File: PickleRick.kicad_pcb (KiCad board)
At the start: 4 copper layers, 100 x 37 mm, 171 parts, among them J1 RBUS, J10 Conn_Coaxial, J11 Conn_Coaxial, J12 Conn_01x03_Male, J2 Conn_01x02_Male, J3 292227-7, J4 Micro_SD_Card_Det, J5 USB_C_Receptacle_USB2.0, J6 Screw_Terminal_01x08, J7 Conn_01x05_Male, J8 DeployLipo, J9 UCLipo, Q1 PMV20ENR, Q2 NCV8415STT1G, Q3 NCV8415STT1G, Q4 NCV8415STT1G, Q5 NCV8415STT1G, Q6 SI4143DY-T1-GE3, Q7 SI4143DY-T1-GE3, U1 ESP32-S3, U10 NCP1117-3.3_SOT223, U11 XC8111, U12 XC8111, U13 XC8111, U14 LTC4412xS6, U15 MAX77827AEFD+T, U16 SC4215, U17 LTC4412xS6, U18 XC8111, U19 MAX-M10S, U2 DPS310, U20 SN65HVD230, U21 RFM95W-868S2, U3 LTV-247, U4 PCA9534RGVR, U5 PCA9685BS, U6 H3LIS331DLTR, U7 ICM-20608-G, U8 MMC5983MA, U9 XC8111, Y1 40MHz±10ppm

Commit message: made more progress
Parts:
- removed C37: 100nF, Capacitor_SMD:C_0402_1005Metric
- removed R13: 10k, Resistor_SMD:R_0402_1005Metric
- J5: footprint Connector_USB:USB_C_Receptacle_GCT_USB4085 -> Connector_USB:USB_C_Receptacle_Palconn_UTC16-G
- TP7, TP8: moved to F.Cu
- moved TP15 152.0 mm to (123.6, 67.4)
- moved TP6 129.4 mm to (123.5, 75.6)
- moved TP5 118.9 mm to (123.5, 73.6)
- moved TP1 103.5 mm to (136.2, 116.6)
- moved TP4 103.5 mm to (131.8, 116.6)
- moved TP10 103.5 mm to (121.4, 114.7)
- moved TP11 103.5 mm to (155.2, 114.3)
- moved TP12 103.5 mm to (154.7, 117.9)
- moved TP13 103.5 mm to (151.2, 116.8)
- moved TP14 103.5 mm to (158.7, 114.3)
- moved TP3 103.5 mm to (144.1, 116.6)
- moved TP9 103.5 mm to (145.0, 110.1)
- moved C48 67.1 mm to (208.9, 93.7), turned to -90 degrees
- moved C47 63.4 mm to (204.0, 88.9), turned to -90 degrees
- moved C46 61.8 mm to (206.5, 88.8), turned to -90 degrees
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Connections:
- J3 pad 1: +3V3 -> /SD2_DET
- J3 pad 3: /VSPI_MOSI -> /VSPI_MISO
- J3 pad 6: /VSPI_MISO -> /VSPI_MOSI
- J3 pad 7: /SD2_DET -> +3V3
- R10 pad 1: +12V -> +24V
- U1 pad 10: /IMU2_CS -> /SD2_DET
- U1 pad 11: /IMU1_CS -> /SD2_CS
- U1 pad 12: /BARO_CS -> /SD1_CS
- U1 pad 16: /SD2_DET -> /IMU2_CS
- U1 pad 17: /SD2_CS -> /IMU1_CS
- U1 pad 18: /SD1_DET -> /MAG_CS
- U1 pad 19: /SD1_CS -> /BARO_CS
- U1 pad 38: /VSPI_MOSI -> /HSPI_SCLK
- U1 pad 39: /VSPI_SCLK -> /HSPI_MOSI
- U1 pad 40: /VSPI_MISO -> /HSPI_MISO
- U1 pad 41: /HSPI_SCLK -> /VSPI_MISO
- U1 pad 42: /HSPI_MOSI -> /VSPI_SCLK
- U1 pad 43: /HSPI_MISO -> /VSPI_MOSI
- U1 pad 9: /MAG_CS -> /SD1_DET
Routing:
- net /SDA: track 7.53 -> 140.9 mm, vias 0 -> 2
- net /SD1_DET: track 0.45 -> 98.0 mm
- net /SD2_DET: track 0.67 -> 97.4 mm
- net /SD2_CS: track 0.00 -> 67.4 mm
- net /LORA_INT: track 23.1 -> 82.0 mm
- net /SCL: track 194.5 -> 143.7 mm, vias 3 -> 2
- net Net-(D7-Pad3): track 54.1 -> 12.6 mm
- net /SD1_CS: track 3.66 -> 43.6 mm
- net VBUS: track 46.9 -> 7.75 mm
- net /HSPI_MOSI: track 31.2 -> 69.3 mm, vias 2 -> 4
- net /HSPI_MISO: track 35.4 -> 71.8 mm, vias 2 -> 4
- net /HSPI_SCLK: track 28.3 -> 63.1 mm, vias 2 -> 4
- net /LORA_RESET: track 20.4 -> 51.4 mm
- net /BARO_CS: track 0.00 -> 30.3 mm
- net /nukes/Nuke1-: track 0.00 -> 27.9 mm
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
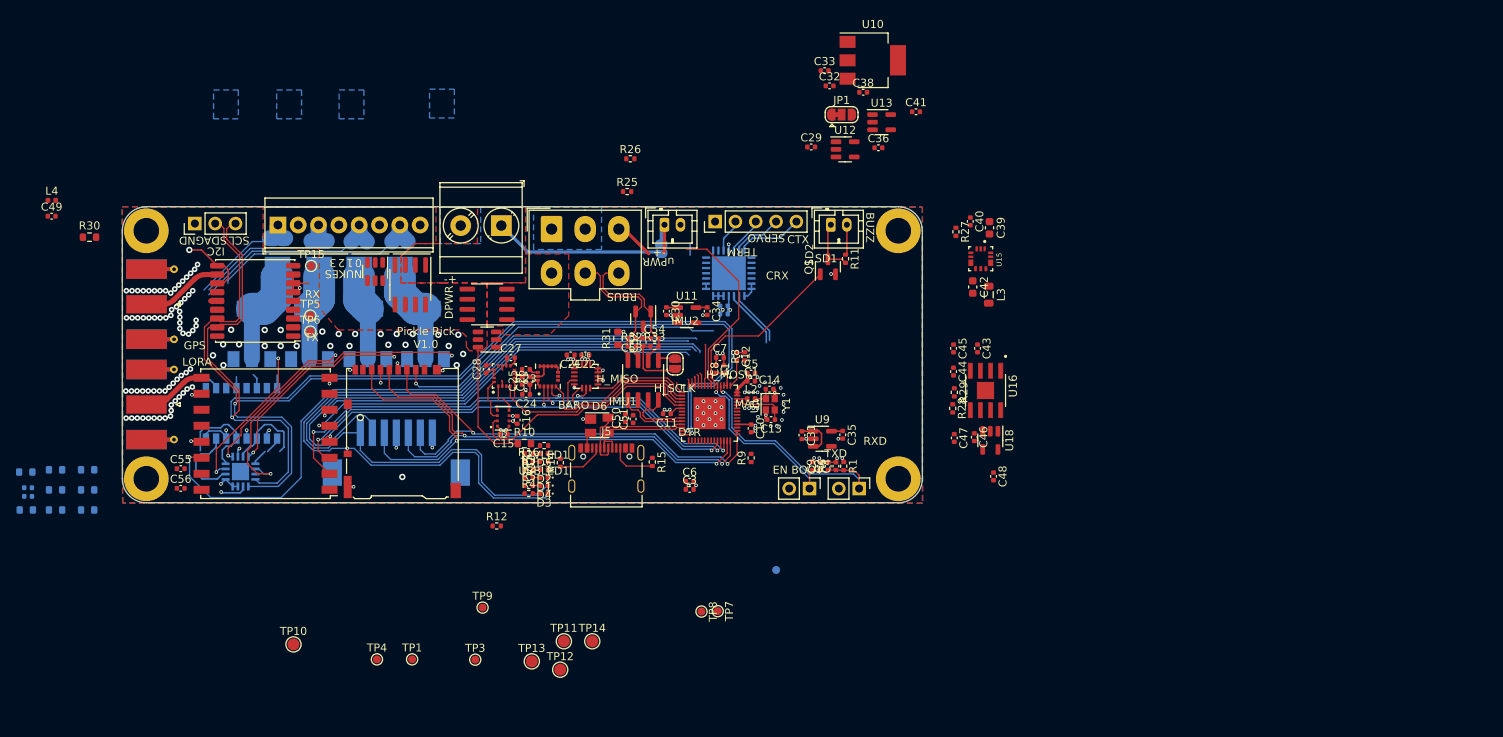
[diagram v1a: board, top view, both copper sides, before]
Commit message: all components basically routed and fitted onto pickle v2
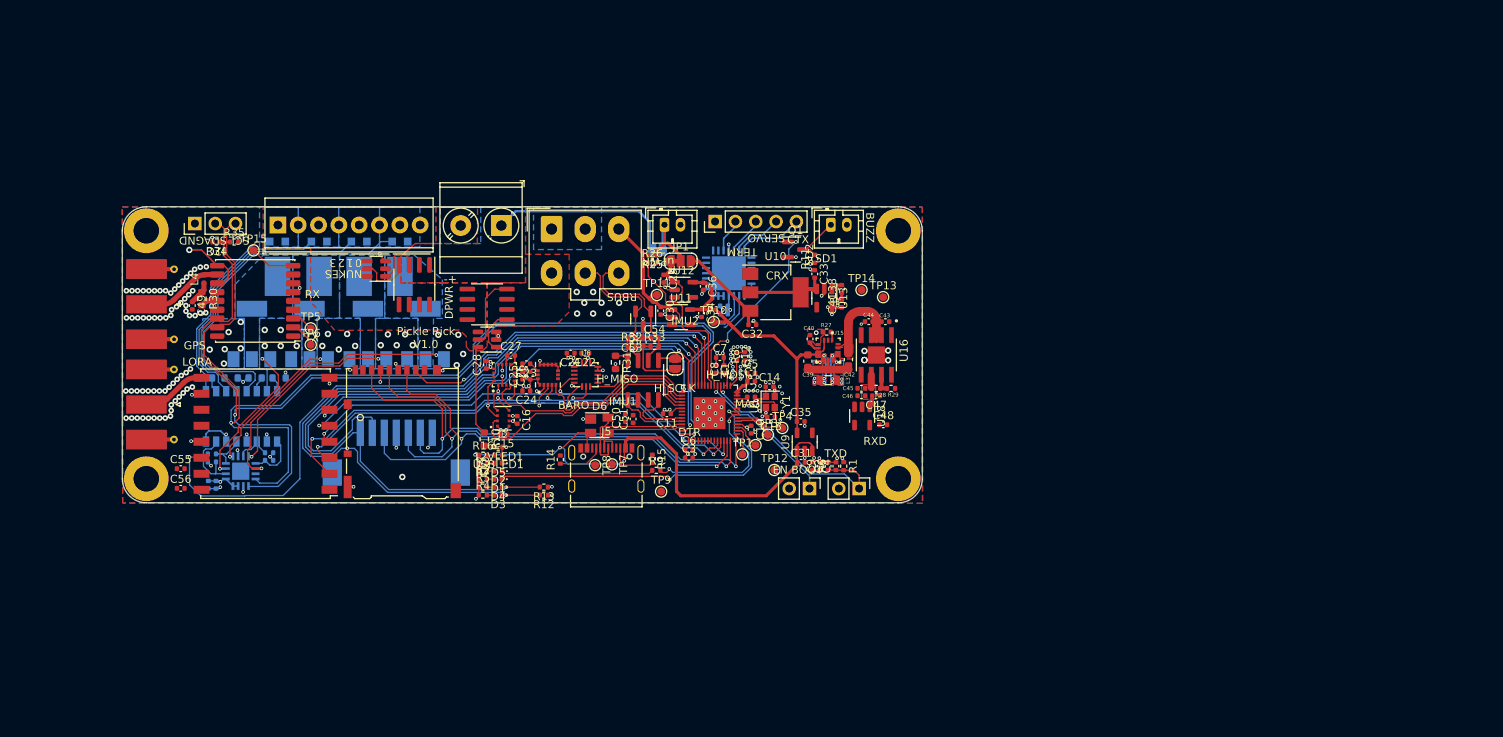
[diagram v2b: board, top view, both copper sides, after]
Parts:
- added R13: 10k, Resistor_SMD:R_0402_1005Metric, F.Cu at (152.7, 95.0)
- added R34: 4.7k, Resistor_SMD:R_0402_1005Metric, F.Cu at (111.8, 64.4)
- added R35: 4.7k, Resistor_SMD:R_0402_1005Metric, F.Cu at (114.0, 64.4)
- R17, R18, R21, R22: footprint Resistor_SMD:R_0603_1608Metric -> Resistor_SMD:R_0402_1005Metric
- TP10, TP11, TP12, TP13, TP14: footprint TestPoint:TestPoint_Pad_D1.5mm -> TestPoint:TestPoint_Pad_D1.0mm
- TP2: moved to F.Cu
- moved TP10 66.2 mm to (173.9, 74.4)
- moved TP13 63.3 mm to (195.1, 71.3)
- moved TP4 58.3 mm to (182.5, 87.7)
- moved TP14 55.3 mm to (192.4, 70.4)
- moved TP1 48.6 mm to (177.5, 91.0)
- moved TP3 46.1 mm to (180.7, 88.5)
- moved TP11 44.8 mm to (166.8, 71.0)
- moved TP12 36.6 mm to (181.5, 92.9)
- moved R23 32.5 mm to (119.6, 81.4), turned to 0 degrees
- moved U10 31.5 mm to (181.7, 70.7)
- moved C32 31.4 mm to (178.8, 74.8), turned to 180 degrees
- moved R20 30.5 mm to (113.6, 81.4), turned to 0 degrees
- moved C39 28.2 mm to (185.7, 79.3)
- moved C36 27.9 mm to (172.6, 70.0), turned to -90 degrees
- moved R24 27.5 mm to (116.6, 81.4)
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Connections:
- J1 pad 3: /RBUS_3.3_IN -> /power/RBUS_3.3V_IN
- J3 pad 3: /VSPI_MISO -> /VSPI_MOSI
- J3 pad 6: /VSPI_MOSI -> /VSPI_MISO
- U1 pad 10: /SD2_DET -> /LORA_INT
- U1 pad 11: /SD2_CS -> /SD1_DET
- U1 pad 12: /SD1_CS -> /SD2_DET
- U1 pad 13: /LORA_CS -> /SD2_CS
- U1 pad 15: /LORA_INT -> /LORA_CS
- U1 pad 38: /HSPI_SCLK -> /HSPI_MOSI
- U1 pad 39: /HSPI_MOSI -> /HSPI_MISO
- U1 pad 40: /HSPI_MISO -> /HSPI_SCLK
- U1 pad 41: /VSPI_MISO -> /VSPI_MOSI
- U1 pad 43: /VSPI_MOSI -> /VSPI_MISO
- U1 pad 9: /SD1_DET -> /SD1_CS
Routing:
- net VBUS: track 7.75 -> 66.1 mm, vias 0 -> 4
- net /RXD: track 0.00 -> 41.3 mm, vias 0 -> 2
- net /power/BBIN: track 2.85 -> 38.6 mm
- net GND: track 65.2 -> 87.5 mm, vias 166 -> 217
- net Net-(R9-Pad2): track 0.00 -> 20.0 mm, vias 0 -> 2
- net /TXD: track 0.00 -> 19.1 mm
- net /nukes/Nuke1-: track 27.9 -> 44.9 mm
- net /power/RBUS_3.3V_IN: track 1.42 -> 18.0 mm
- net /nukes/Nuke2-: track 25.5 -> 39.2 mm
- net Net-(C33-Pad2): track 0.00 -> 13.6 mm
- net Net-(D7-Pad3): track 12.6 -> 0.00 mm
- net Net-(D10-Pad3): track 12.4 -> 0.00 mm
- net /power/BBOUT: track 0.00 -> 12.3 mm
- net Net-(C32-Pad2): track 0.00 -> 11.8 mm
- net /nukes/Nuke3-: track 19.2 -> 30.2 mm
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- added copper zone on F.Cu, net (none)
- added copper zone on F.Cu, net +3V3
- added copper zone on B.Cu, net /nukes/Nuke1-
- added copper zone on B.Cu, net /nukes/Nuke2-
- added copper zone on B.Cu, net /nukes/Nuke3-
- added copper zone on B.Cu, net /nukes/Nuke4-
- added copper zone on F.Cu, net /power/BBOUT
- added copper zone on B.Cu, net /power/LX1
- added copper zone on F.Cu, net /power/LX1
- added copper zone on B.Cu, net /power/LX2
- added copper zone on F.Cu, net /power/LX2
- added copper zone on B.Cu, net Net-(D10-Pad3)
- added copper zone on B.Cu, net Net-(D7-Pad3)
- added copper zone on B.Cu, net Net-(D8-Pad3)
- added copper zone on B.Cu, net Net-(D9-Pad3)

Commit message: minor updates
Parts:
- moved C51 0.78 mm to (163.1, 86.3)
- moved C50 0.71 mm to (162.2, 86.3)
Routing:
- net +3V3: track 57.8 -> 62.6 mm, vias 34 -> 39
- net Net-(C45-Pad2): track 3.13 -> 6.29 mm
- net GND: track 87.5 -> 89.1 mm, vias 217 -> 219
- added copper zone on F.Cu, net Net-(C45-Pad2)
- removed copper zone on F.Cu, net +3V3
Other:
- board text added: "Designed By Kiran de Silva Electronics & Payload 2023"
- board text added: "Pickle Rick V2.0"
- board text removed: "Designed By Kiran de Silva Electronics & Payload 2022"
- board text removed: "Pickle Rick V1.0"

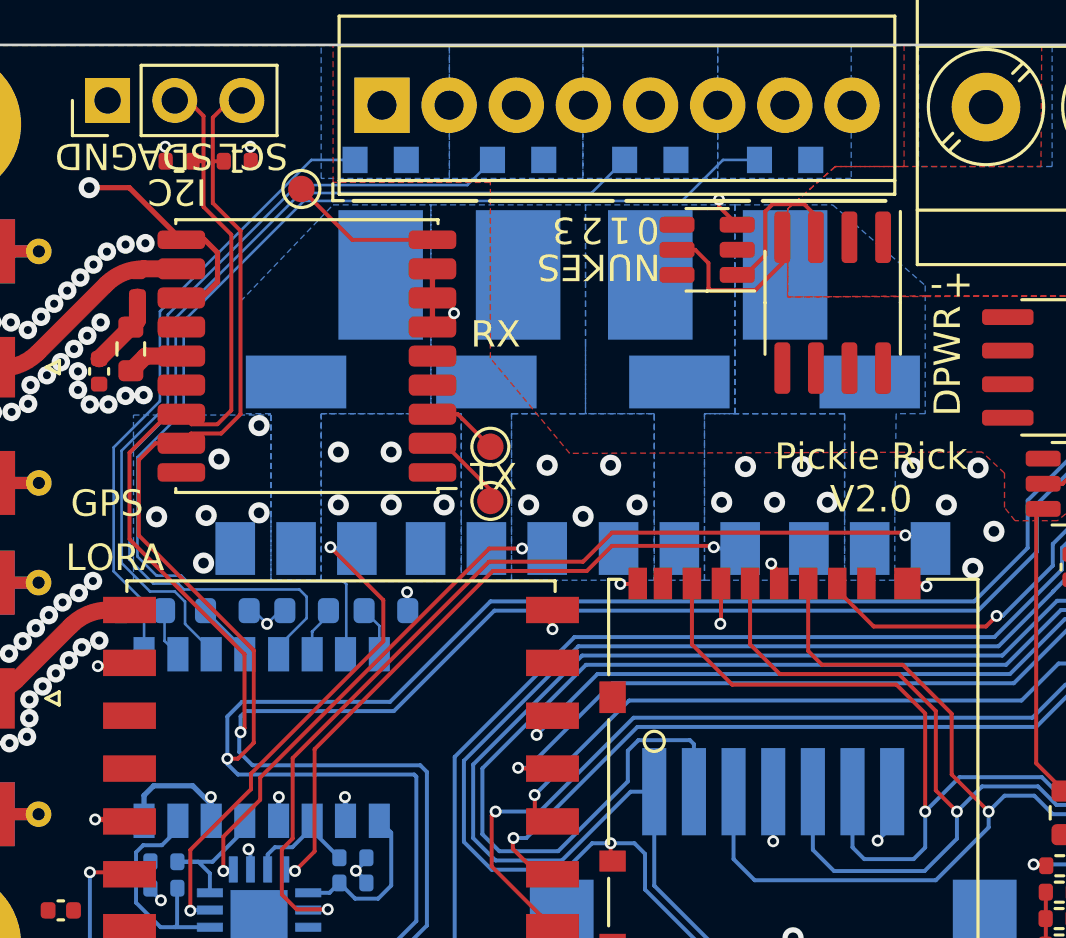
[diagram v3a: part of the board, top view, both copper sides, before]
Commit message: converted to kicad 7
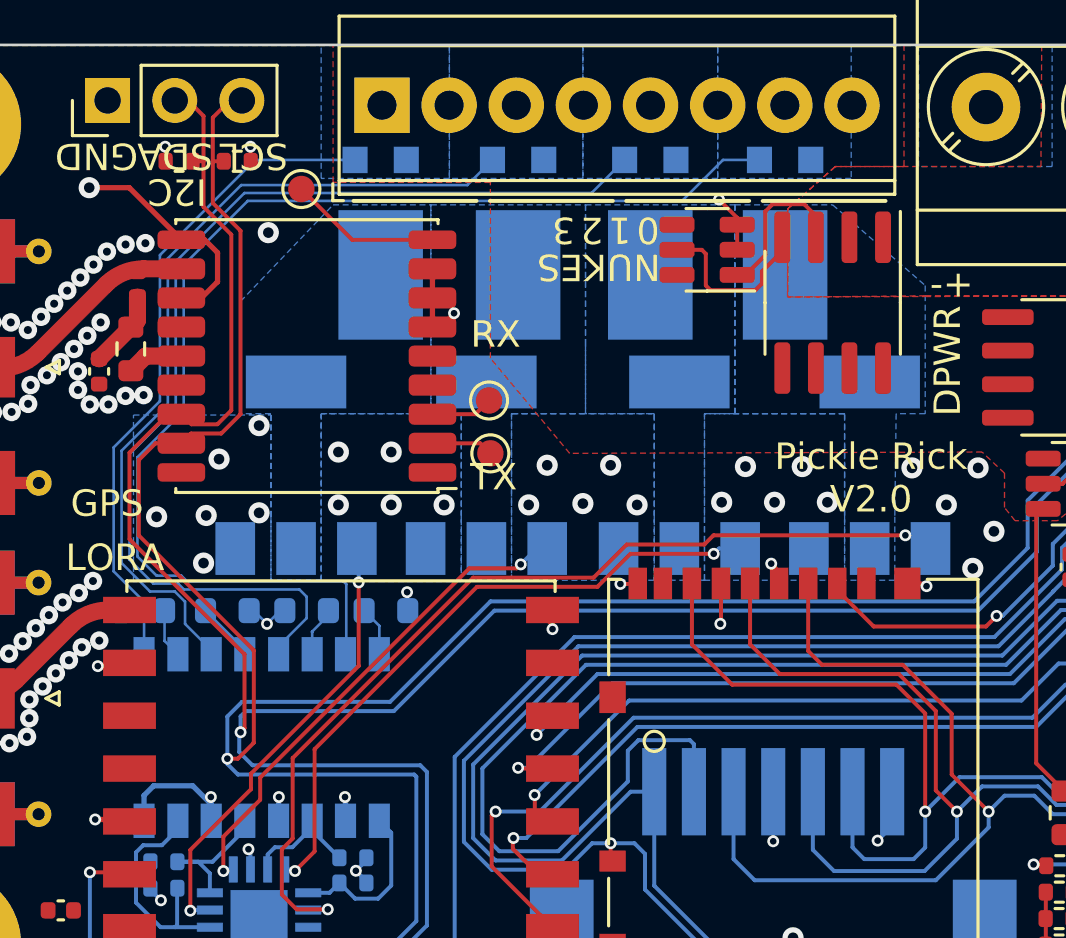
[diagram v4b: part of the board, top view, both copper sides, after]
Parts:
- moved TP6 1.80 mm to (123.5, 75.5)
- moved TP5 1.75 mm to (123.5, 73.5)
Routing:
- net /nukes/Nuke4: track 19.4 -> 17.1 mm
- net /nukes/Nuke4-: track 23.9 -> 25.2 mm
- net /nukes/Nuke3-: track 30.2 -> 31.5 mm
- net /nukes/Nuke2-: track 39.2 -> 40.5 mm
- net /nukes/Nuke1-: track 44.9 -> 46.2 mm
- net /GPS/TXD: track 3.34 -> 2.35 mm
- net GND: track 89.1 -> 90.1 mm, vias 219 -> 220

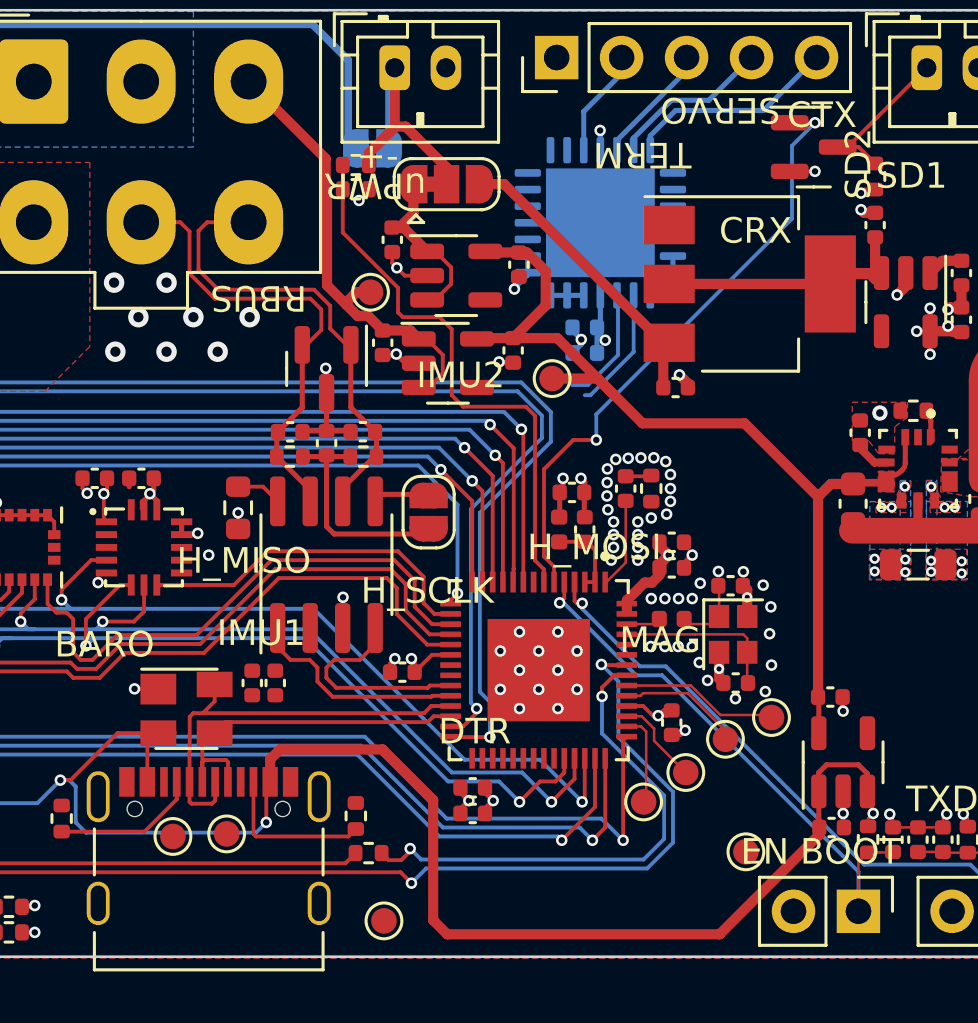
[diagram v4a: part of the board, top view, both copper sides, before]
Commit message: changed bb and power side
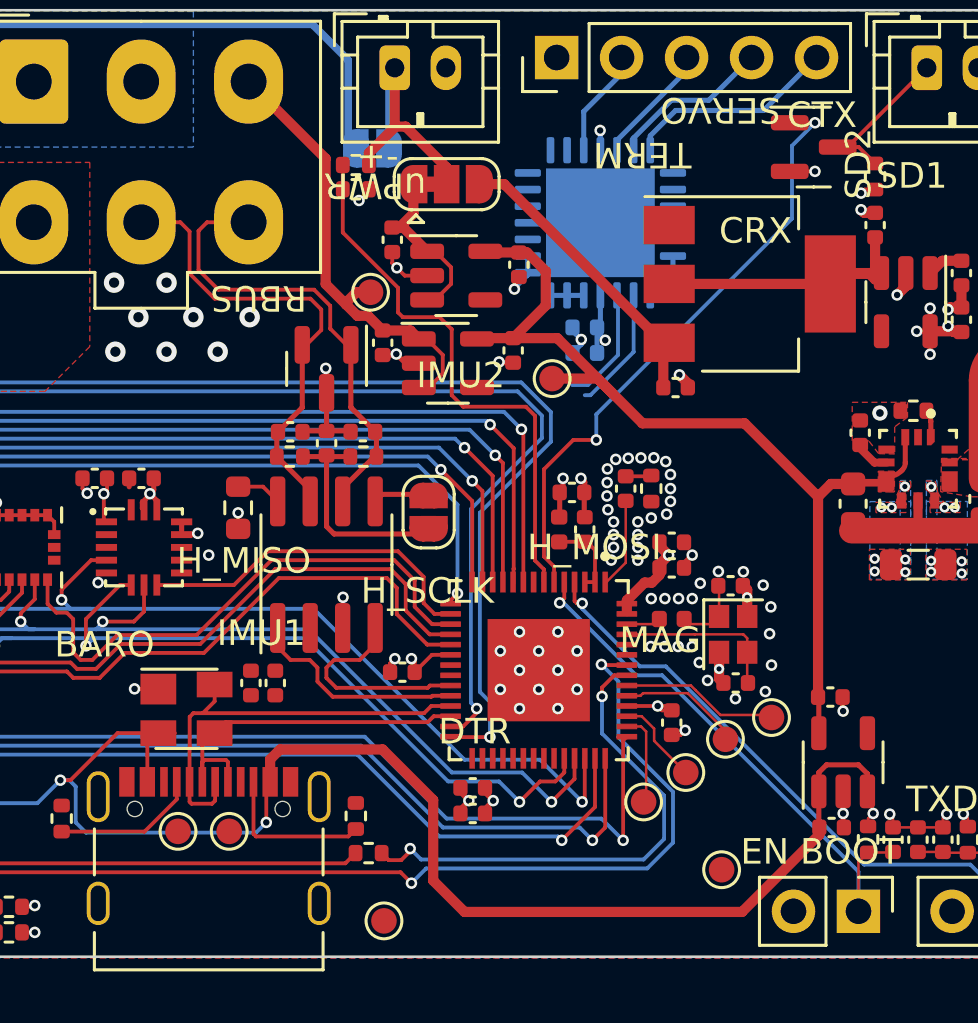
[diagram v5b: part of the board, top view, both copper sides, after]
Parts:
- moved TP8 2.21 mm to (161.3, 92.1)
- moved TP7 1.90 mm to (159.3, 92.1)
- moved TP12 1.18 mm to (180.6, 93.6)
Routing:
- net VBUS: track 66.1 -> 64.4 mm
